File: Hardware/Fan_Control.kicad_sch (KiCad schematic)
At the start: 20 parts, among them Q1 PSMN8R5-40MSDX, Q3 PSMN8R5-40MSDX, U3 EMC2305-1-AP-TR

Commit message: revB updates
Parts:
- removed Fan1, Fan2: Conn_01x03, Connector_Molex:Molex_Nano-Fit_105309-xx03_1x03_P2.50mm_Vertical, symbol Connector_Generic:Conn_01x03
- removed Q1, Q3: PSMN8R5-40MSDX, UTSVT_Power:PSMN8R5-40MSDX, symbol Transistor_FET:BUK7M27-80EX
- removed R1, R12: 10k, Resistor_SMD:R_0603_1608Metric, symbol Device:R_US
- removed R16, R17: 100k, Resistor_SMD:R_0603_1608Metric, symbol Device:R_US
- removed R3, R4: 5.1k, Resistor_SMD:R_0603_1608Metric, symbol Device:R_US
- added FAN1, FAN2: Conn_01x04, symbol Connector_Generic:Conn_01x04
- added R84, R85: 5.1k, Resistor_SMD:R_0603_1608Metric, symbol Device:R_US
- D4, D7: footprint (none) -> VSSAF522-M3/H:SODFL5226X100N
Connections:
- net FAN_1_FLYBACK is gone; now on net GND: D4.2 (A)
- net FAN_2_FLYBACK is gone; now on net GND: D7.2 (A)
- net +24V: now also FAN1.1 (Pin_1), FAN2.1 (Pin_1)
- net +3.3V: now also R84.1, R85.1
- net FAN_1_PWM: now also FAN1.3 (Pin_3)
- net FAN_1_TACH: now also FAN1.2 (Pin_2), R84.2
- net FAN_2_PWM: now also FAN2.3 (Pin_3)
- net FAN_2_TACH: now also FAN2.2 (Pin_2), R85.2
- net GND: now also FAN1.4 (Pin_4), FAN2.4 (Pin_4)
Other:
- note removed: "Pull-Down Resistors"
- note removed: "Test to see if 100k pulldowns nessasaey"
- moved on the sheet: D4, D7

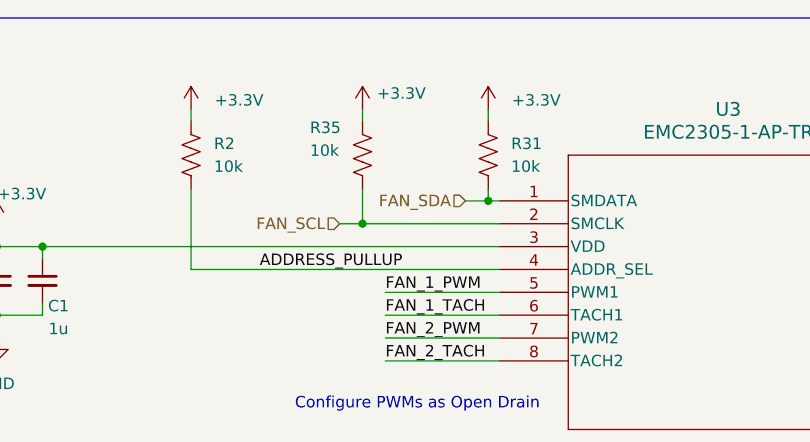
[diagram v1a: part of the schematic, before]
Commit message: Schematic polishes, layout WIP
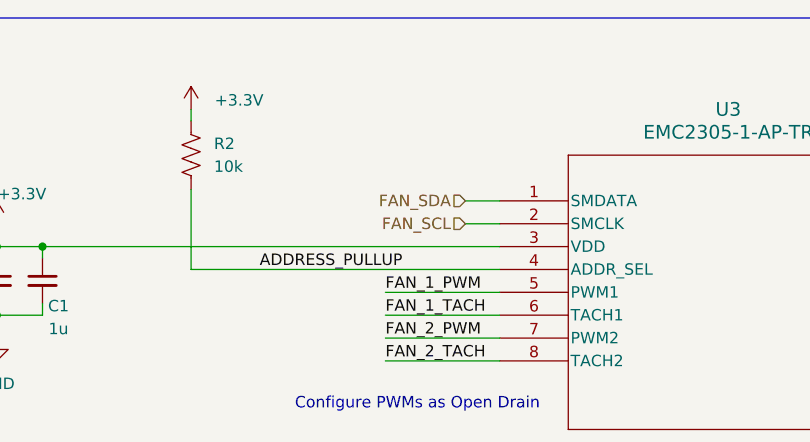
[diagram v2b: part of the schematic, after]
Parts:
- removed R31, R35: 10k, Resistor_SMD:R_0603_1608Metric, symbol Device:R_US
- FAN1, FAN2: footprint (none) -> Connector_Molex:Molex_Nano-Fit_105309-xx04_1x04_P2.50mm_Vertical

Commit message: circuit blocks designed, schematic updated
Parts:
- removed R5: 10k, Resistor_SMD:R_0603_1608Metric, symbol Device:R_US
- R13, R2: value 10k -> 33k
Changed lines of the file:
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@@
-		(color 0 0 0 0)
-	)
-	(junction
-		(at 154.94 49.53)
-		(diameter 0)
 		(color 0 0 0 0)
 	)
@@
 	(wire
 		(pts
-			(xy 154.94 49.53) (xy 157.48 49.53)
+			(xy 151.13 49.53) (xy 157.48 49.53)
 		)
 		(stroke
@@
 	(wire
 		(pts
-			(xy 154.94 48.26) (xy 154.94 49.53)
-		)
-		(stroke
-			(width 0)
-			(type default)
-		)
-	)
-	(wire
-		(pts
 			(xy 185.42 52.07) (xy 185.42 50.8)
 		)
@@
 		(pts
 			(xy 87.63 54.61) (xy 100.33 54.61)
-		)
-		(stroke
-			(width 0)
-			(type default)
-		)
-	)
-	(wire
-		(pts
-			(xy 151.13 49.53) (xy 154.94 49.53)
 		)
 		(stroke
@@
 	)
 	(symbol
-		(lib_id "power:+3.3V")
-		(at 154.94 40.64 0)
-		(unit 1)
-		(exclude_from_sim no)
-		(in_bom yes)
-		(on_board yes)
-		(dnp no)
-		(property "Reference" "#PWR016"
-			(at 154.94 44.45 0)
-			(effects
-				(font
-					(size 1.27 1.27)
-				)
-				(hide yes)
-			)
-		)
-		(property "Value" "+3.3V"
-			(at 158.75 39.37 0)
-			(effects
-				(font
-					(size 1.27 1.27)
-				)
-			)
-		)
-		(property "Footprint" ""
-			(at 154.94 40.64 0)
-			(effects
-				(font
-					(size 1.27 1.27)
-				)
-				(hide yes)
-			)
-		)
-		(property "Datasheet" ""
-			(at 154.94 40.64 0)
-			(effects
-				(font
-					(size 1.27 1.27)
-				)
-				(hide yes)
-			)
-		)
-		(property "Description" "Power symbol creates a global label with name \"+3.3V\""
-			(at 154.94 40.64 0)
-			(effects
-				(font
-					(size 1.27 1.27)
-				)
-				(hide yes)
-			)
-		)
-		(pin "1"
-		)
-		(instances
-			(project "BPS-Leader"
-				(path "/fb37da34-e420-4994-8cc1-079e8c0fa48e/8d0cbdc7-6b16-43b7-9a81-5c7e9e7d19f5"
-					(reference "#PWR016")
-					(unit 1)
-				)
-			)
-		)
-	)
-	(symbol
 		(lib_id "power:+24V")
 		(at 177.8 96.52 0)
@@
 				(path "/fb37da34-e420-4994-8cc1-079e8c0fa48e/8d0cbdc7-6b16-43b7-9a81-5c7e9e7d19f5"
 					(reference "D4")
-					(unit 1)
-				)
-			)
-		)
-	)
-	(symbol
-		(lib_id "Device:R_US")
-		(at 154.94 44.45 0)
-		(unit 1)
-		(exclude_from_sim no)
-		(in_bom yes)
-		(on_board yes)
-		(dnp no)
-		(fields_autoplaced yes)
-		(property "Reference" "R5"
-			(at 157.48 43.1799 0)
-			(effects
-				(font
-					(size 1.27 1.27)
-				)
-				(justify left)
-			)
-		)
-		(property "Value" "10k"
-			(at 157.48 45.7199 0)
-			(effects
-				(font
-					(size 1.27 1.27)
-				)
-				(justify left)
-			)
-		)
-		(property "Footprint" "Resistor_SMD:R_0603_1608Metric"
-			(at 155.956 44.704 90)
-			(effects
-				(font
-					(size 1.27 1.27)
-				)
-				(hide yes)
-			)
-		)
-		(property "Datasheet" "https://www.vishay.com/docs/20035/dcrcwe3.pdf"
-			(at 154.94 44.45 0)
-			(effects
-				(font
-					(size 1.27 1.27)
-				)
-				(hide yes)
-			)
-		)
-		(property "Description" "Resistor, US symbol"
-			(at 154.94 44.45 0)
-			(effects
-				(font
-					(size 1.27 1.27)
-				)
-				(hide yes)
-			)
-		)
-		(property "Manufactuerer" "Vishay "
-			(at 154.94 44.45 0)
-			(effects
-				(font
-					(size 1.27 1.27)
-				)
-				(hide yes)
-			)
-		)
-		(property "P/N" "CRCW060310K0FKEI "
-			(at 154.94 44.45 0)
-			(effects
-				(font
-					(size 1.27 1.27)
-				)
-				(hide yes)
-			)
-		)
-		(pin "1"
-		)
-		(pin "2"
-		)
-		(instances
-			(project "BPS-Leader"
-				(path "/fb37da34-e420-4994-8cc1-079e8c0fa48e/8d0cbdc7-6b16-43b7-9a81-5c7e9e7d19f5"
-					(reference "R5")
 					(unit 1)
 				)
@@
 			)
 		)
-		(property "Value" "10k"
+		(property "Value" "33k"
 			(at 187.96 48.2599 0)
 			(effects
@@
 			)
 		)
-		(property "Value" "10k"
+		(property "Value" "33k"
 			(at 68.58 33.0199 0)
 			(effects

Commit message: intial layout design
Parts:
- R84, R85: value 5.1k -> 10k
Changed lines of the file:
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@@
-	(wire
-		(pts
-			(xy 177.8 107.95) (xy 177.8 106.68)
-		)
-		(stroke
-			(width 0)
-			(type default)
-		)
-	)
 	(wire
 		(pts
@@
 	(wire
 		(pts
-			(xy 123.19 109.22) (xy 140.97 109.22)
-		)
-		(stroke
-			(width 0)
-			(type default)
-		)
-	)
-	(wire
-		(pts
 			(xy 151.13 52.07) (xy 185.42 52.07)
 		)
@@
 	(wire
 		(pts
+			(xy 177.8 106.68) (xy 177.8 111.76)
+		)
+		(stroke
+			(width 0)
+			(type default)
+		)
+	)
+	(wire
+		(pts
 			(xy 33.02 101.6) (xy 33.02 97.79)
 		)
@@
 	(wire
 		(pts
-			(xy 140.97 106.68) (xy 140.97 109.22)
+			(xy 140.97 106.68) (xy 140.97 111.76)
 		)
 		(stroke
@@
 		(pts
 			(xy 44.45 41.91) (xy 44.45 43.18)
-		)
-		(stroke
-			(width 0)
-			(type default)
-		)
-	)
-	(wire
-		(pts
-			(xy 160.02 107.95) (xy 177.8 107.95)
 		)
 		(stroke
@@
 		)
 	)
-	(label "FAN_2_FLYBACK"
-		(at 160.02 107.95 0)
-		(effects
-			(font
-				(size 1.27 1.27)
-			)
-			(justify left bottom)
-		)
-	)
 	(label "FAN_2_TACH"
 		(at 74.93 101.6 0)
@@
 		)
 	)
-	(label "FAN_2_FLYBACK"
-		(at 72.39 106.68 0)
-		(effects
-			(font
-				(size 1.27 1.27)
-			)
-			(justify left bottom)
-		)
-	)
 	(label "FAN_2_PWM"
 		(at 87.63 52.07 0)
-		(effects
-			(font
-				(size 1.27 1.27)
-			)
-			(justify left bottom)
-		)
-	)
-	(label "FAN_1_FLYBACK"
-		(at 123.19 109.22 0)
-		(effects
-			(font
-				(size 1.27 1.27)
-			)
-			(justify left bottom)
-		)
-	)
-	(label "FAN_1_FLYBACK"
-		(at 33.02 106.68 0)
 		(effects
 			(font
@@
 	)
 	(symbol
+		(lib_id "power:GND")
+		(at 140.97 111.76 0)
+		(unit 1)
+		(exclude_from_sim no)
+		(in_bom yes)
+		(on_board yes)
+		(dnp no)
+		(property "Reference" "#PWR0112"
+			(at 140.97 118.11 0)
+			(effects
+				(font
+					(size 1.27 1.27)
+				)
+				(hide yes)
+			)
+		)
+		(property "Value" "GND"
+			(at 138.176 111.76 0)
+			(effects
+				(font
+					(size 1.27 1.27)
+				)
+			)
+		)
+		(property "Footprint" ""
+			(at 140.97 111.76 0)
+			(effects
+				(font
+					(size 1.27 1.27)
+				)
+				(hide yes)
+			)
+		)
+		(property "Datasheet" ""
+			(at 140.97 111.76 0)
+			(effects
+				(font
+					(size 1.27 1.27)
+				)
+				(hide yes)
+			)
+		)
+		(property "Description" "Power symbol creates a global label with name \"GND\" , ground"
+			(at 140.97 111.76 0)
+			(effects
+				(font
+					(size 1.27 1.27)
+				)
+				(hide yes)
+			)
+		)
+		(pin "1"
+		)
+		(instances
+			(project "BPS-Leader"
+				(path "/fb37da34-e420-4994-8cc1-079e8c0fa48e/8d0cbdc7-6b16-43b7-9a81-5c7e9e7d19f5"
+					(reference "#PWR0112")
+					(unit 1)
+				)
+			)
+		)
+	)
+	(symbol
 		(lib_id "Device:C_Small")
 		(at 44.45 45.72 0)
@@
 			)
 		)
-		(property "Value" "5.1k"
+		(property "Value" "10k"
 			(at 35.56 95.2499 0)
 			(effects
@@
 				(path "/fb37da34-e420-4994-8cc1-079e8c0fa48e/8d0cbdc7-6b16-43b7-9a81-5c7e9e7d19f5"
 					(reference "R84")
+					(unit 1)
+				)
+			)
+		)
+	)
+	(symbol
+		(lib_id "power:GND")
+		(at 177.8 111.76 0)
+		(unit 1)
+		(exclude_from_sim no)
+		(in_bom yes)
+		(on_board yes)
+		(dnp no)
+		(property "Reference" "#PWR0118"
+			(at 177.8 118.11 0)
+			(effects
+				(font
+					(size 1.27 1.27)
+				)
+				(hide yes)
+			)
+		)
+		(property "Value" "GND"
+			(at 175.006 111.76 0)
+			(effects
+				(font
+					(size 1.27 1.27)
+				)
+			)
+		)
+		(property "Footprint" ""
+			(at 177.8 111.76 0)
+			(effects
+				(font
+					(size 1.27 1.27)
+				)
+				(hide yes)
+			)
+		)
+		(property "Datasheet" ""
+			(at 177.8 111.76 0)
+			(effects
+				(font
+					(size 1.27 1.27)
+				)
+				(hide yes)
+			)
+		)
+		(property "Description" "Power symbol creates a global label with name \"GND\" , ground"
+			(at 177.8 111.76 0)
+			(effects
+				(font
+					(size 1.27 1.27)
+				)
+				(hide yes)
+			)
+		)
+		(pin "1"
+		)
+		(instances
+			(project "BPS-Leader"
+				(path "/fb37da34-e420-4994-8cc1-079e8c0fa48e/8d0cbdc7-6b16-43b7-9a81-5c7e9e7d19f5"
+					(reference "#PWR0118")
 					(unit 1)
 				)
@@
 			)
 		)
-		(property "Value" "5.1k"
+		(property "Value" "10k"
 			(at 74.93 95.2499 0)
 			(effects

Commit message: JLC Production Files
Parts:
- C1, C2: LCSC (none) -> C15849
- D4, D7: LCSC (none) -> C6326606
- R13, R2: LCSC (none) -> C844778
- R84, R85: LCSC (none) -> C25804
- U3: LCSC (none) -> C621415
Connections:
- net GND: now also U3.17 (EPAD); no longer U3.HTAB (EPAD)
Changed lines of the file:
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@@
+			)
+		)
+		(property "LCSC" "C6326606"
+			(at 180.34 100.33 0)
+			(effects
+				(font
+					(size 1.27 1.27)
+				)
+				(hide yes)
 			)
 		)
@@
 		(property "P/N" "VSSAF522-M3/H"
 			(at 140.97 102.87 90)
+			(effects
+				(font
+					(size 1.27 1.27)
+				)
+				(hide yes)
+			)
+		)
+		(property "LCSC" "C6326606"
+			(at 143.51 100.33 0)
 			(effects
 				(font
@@
 			)
 		)
+		(property "LCSC" "C844778"
+			(at 187.96 45.7199 0)
+			(effects
+				(font
+					(size 1.27 1.27)
+				)
+				(hide yes)
+			)
+		)
 		(pin "1"
 		)
@@
 			)
 		)
+		(property "LCSC" "C621415"
+			(at 125.73 26.67 0)
+			(effects
+				(font
+					(size 1.27 1.27)
+				)
+				(hide yes)
+			)
+		)
 		(pin "8"
 		)
@@
 		(pin "6"
 		)
-		(pin "HTAB"
+		(pin "17"
 		)
 		(pin "13"
@@
 			)
 		)
+		(property "LCSC" "C844778"
+			(at 68.58 30.4799 0)
+			(effects
+				(font
+					(size 1.27 1.27)
+				)
+				(hide yes)
+			)
+		)
 		(pin "1"
 		)
@@
 			)
 		)
+		(property "LCSC" "C15849"
+			(at 40.64 44.958 0)
+			(effects
+				(font
+					(size 1.27 1.27)
+				)
+				(hide yes)
+			)
+		)
 		(pin "2"
 		)
@@
 			)
 		)
+		(property "LCSC" "C25804"
+			(at 35.56 92.7099 0)
+			(effects
+				(font
+					(size 1.27 1.27)
+				)
+				(hide yes)
+			)
+		)
 		(pin "1"
 		)
@@
 		(property "Manufactuerer" "TAIYO YUDEN "
 			(at 49.53 45.72 0)
+			(effects
+				(font
+					(size 1.27 1.27)
+				)
+				(hide yes)
+			)
+		)
+		(property "LCSC" "C15849"
+			(at 51.308 48.514 0)
 			(effects
 				(font
@@
 			(effects
 				(font
+					(size 1.27 1.27)
+				)
+				(hide yes)
+			)
+		)
+		(property "LCSC" "C25804"
+			(at 74.93 92.7099 0)
+			(effects
+				(font

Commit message: condensed custom lirbraries
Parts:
- D4, D7: footprint VSSAF522-M3/H:SODFL5226X100N -> CustomKiCad-Library:SODFL5226X100N
- U3: footprint EMC2305-1-AP-TR:QFN65P400X400X90-17N-D -> CustomKiCad-Library:QFN65P400X400X90-17N-D
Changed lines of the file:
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@@
 			)
 		)
-		(property "Footprint" "VSSAF522-M3/H:SODFL5226X100N"
+		(property "Footprint" "CustomKiCad-Library:SODFL5226X100N"
 			(at 173.355 102.87 0)
 			(effects
@@
 			)
 		)
-		(property "Footprint" "VSSAF522-M3/H:SODFL5226X100N"
+		(property "Footprint" "CustomKiCad-Library:SODFL5226X100N"
 			(at 136.525 102.87 0)
 			(effects
@@
 			)
 		)
-		(property "Footprint" "EMC2305-1-AP-TR:QFN65P400X400X90-17N-D"
+		(property "Footprint" "CustomKiCad-Library:QFN65P400X400X90-17N-D"
 			(at 100.33 36.83 0)
 			(effects

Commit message: JLCPCB ouput files
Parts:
- R84, R85: P/N CRCW06035K10FKEC -> CRCW060310K0FKEI
